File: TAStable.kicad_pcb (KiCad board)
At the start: 2 copper layers, 20 x 16.5 mm, 12 parts, among them J1 Conn_01x06_Pin, U1 74AHCT1G04, U2 CS2300-CP, U3 74LVC1G14

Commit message: schematic
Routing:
- net /21MHz_IN: track 8.04 -> 6.75 mm
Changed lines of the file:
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@@
   (segment (start 128 98.05) (end 128 99.054) (width 0.254) (layer "F.Cu") (net 7))
   (segment (start 132 96.1) (end 132 94.75) (width 0.25) (layer "F.Cu") (net 8))
+  (segment (start 140.24 98.72) (end 140.375 98.72) (width 0.25) (layer "F.Cu") (net 8))
   (segment (start 130.5 93.25) (end 132 94.75) (width 0.254) (layer "F.Cu") (net 8))
-  (segment (start 137.055 97.5) (end 138.275 98.72) (width 0.25) (layer "F.Cu") (net 8))
   (segment (start 132.55 96.65) (end 132 96.1) (width 0.25) (layer "F.Cu") (net 8))
-  (segment (start 138.275 98.72) (end 140.375 98.72) (width 0.25) (layer "F.Cu") (net 8))
+  (segment (start 139.02 97.5) (end 140.24 98.72) (width 0.25) (layer "F.Cu") (net 8))
   (segment (start 128 93.25) (end 130.5 93.25) (width 0.254) (layer "F.Cu") (net 8))
-  (segment (start 135.3 97.5) (end 137.055 97.5) (width 0.25) (layer "F.Cu") (net 8))
   (segment (start 127 94.25) (end 128 93.25) (width 0.254) (layer "F.Cu") (net 8))
   (segment (start 132.55 96.65) (end 134.05 96.65) (width 0.25) (layer "F.Cu") (net 8))
   (segment (start 127 98.05) (end 127 94.25) (width 0.254) (layer "F.Cu") (net 8))
   (segment (start 135.405 97.395) (end 135.3 97.5) (width 0.25) (layer "F.Cu") (net 8))
+  (segment (start 135.3 97.5) (end 139.02 97.5) (width 0.25) (layer "F.Cu") (net 8))
   (segment (start 134.05 96.65) (end 134.795 97.395) (width 0.25) (layer "F.Cu") (net 8))
-  (segment (start 136.4 100.4) (end 136.4 102.6) (width 0.254) (layer "F.Cu") (net 9))
-  (segment (start 138.275 103.8) (end 140.375 103.8) (width 0.25) (layer "F.Cu") (net 9))
-  (segment (start 136.4 102.6) (end 137.6 103.8) (width 0.254) (layer "F.Cu") (net 9))
-  (segment (start 136 100) (end 136.4 100.4) (width 0.254) (layer "F.Cu") (net 9))
-  (segment (start 135.2 100) (end 136 100) (width 0.254) (layer "F.Cu") (net 9))
-  (segment (start 137.6 103.8) (end 138.275 103.8) (width 0.254) (layer "F.Cu") (net 9))
+  (segment (start 140.3 103.8) (end 140.375 103.8) (width 0.25) (layer "F.Cu") (net 9))
+  (segment (start 136.37 100) (end 135.2 100) (width 0.254) (layer "F.Cu") (net 9))
+  (segment (start 136.37 100) (end 136.5 100) (width 0.25) (layer "F.Cu") (net 9))
+  (segment (start 136.5 100) (end 140.3 103.8) (width 0.25) (layer "F.Cu") (net 9))
   (segment (start 131.25 96.5) (end 131.25 95) (width 0.25) (layer "F.Cu") (net 10))
-  (segment (start 136.5 99.5) (end 135.5 98.5) (width 0.25) (layer "F.Cu") (net 10))
-  (segment (start 138.275 101.26) (end 136.515 99.5) (width 0.25) (layer "F.Cu") (net 10))
   (segment (start 133.45 97.5) (end 133.3 97.5) (width 0.25) (layer "F.Cu") (net 10))
+  (segment (start 137.39 98.55) (end 134.35 98.55) (width 0.25) (layer "F.Cu") (net 10))
+  (segment (start 140.375 101.26) (end 140.1 101.26) (width 0.25) (layer "F.Cu") (net 10))
   (segment (start 127.5 94.75) (end 127.5 98.05) (width 0.25) (layer "F.Cu") (net 10))
-  (segment (start 136.515 99.5) (end 136.5 99.5) (width 0.25) (layer "F.Cu") (net 10))
-  (segment (start 133.75 97.5) (end 133.3 97.5) (width 0.25) (layer "F.Cu") (net 10))
+  (segment (start 134.35 98.55) (end 133.3 97.5) (width 0.25) (layer "F.Cu") (net 10))
   (segment (start 130 93.75) (end 128.5 93.75) (width 0.25) (layer "F.Cu") (net 10))
-  (segment (start 138.275 101.26) (end 140.375 101.26) (width 0.25) (layer "F.Cu") (net 10))
   (segment (start 128.5 93.75) (end 127.5 94.75) (width 0.25) (layer "F.Cu") (net 10))
-  (segment (start 134.75 98.5) (end 133.75 97.5) (width 0.25) (layer "F.Cu") (net 10))
-  (segment (start 135.5 98.5) (end 134.75 98.5) (width 0.25) (layer "F.Cu") (net 10))
   (segment (start 133.3 97.5) (end 132.25 97.5) (width 0.25) (layer "F.Cu") (net 10))
   (segment (start 132.25 97.5) (end 131.25 96.5) (width 0.25) (layer "F.Cu") (net 10))
   (segment (start 131.25 95) (end 130 93.75) (width 0.25) (layer "F.Cu") (net 10))
-  (segment (start 135.15 104.8) (end 136.69 106.34) (width 0.254) (layer "F.Cu") (net 11))
-  (segment (start 136.69 106.34) (end 140.375 106.34) (width 0.254) (layer "F.Cu") (net 11))
+  (segment (start 140.1 101.26) (end 137.39 98.55) (width 0.25) (layer "F.Cu") (net 10))
+  (segment (start 135.15 104.8) (end 138.6 104.8) (width 0.254) (layer "F.Cu") (net 11))
+  (segment (start 138.6 104.8) (end 140.14 106.34) (width 0.254) (layer "F.Cu") (net 11))
+  (segment (start 140.14 106.34) (end 140.375 106.34) (width 0.254) (layer "F.Cu") (net 11))
   (zone (net 2) (net_name "GND") (layer "B.Cu") (hatch edge 0.5)
     (connect_pads (clearance 0.5))

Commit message: cleanups
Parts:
- moved C1 0.25 mm to (129.2, 96.0)
- moved C2 0.25 mm to (127.8, 105.5)
- moved C3 0.25 mm to (131.5, 106.0)
- moved C4 0.25 mm to (134.4, 103.1)
- moved C5 0.25 mm to (134.5, 93.2)
- moved R1 0.25 mm to (135.3, 96.9)
- moved R2 0.25 mm to (133.3, 96.9)
- moved R3 0.25 mm to (131.2, 99.5)
- moved U1 0.25 mm to (134.5, 106.0)
- moved U2 0.25 mm to (128.0, 100.5)
- moved U3 0.25 mm to (134.2, 100.2)
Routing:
- net +3.3V: track 61.0 -> 60.2 mm
- added copper zone on F.Cu, net GND

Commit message: code!
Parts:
- added C6: 22uF Tantalum, Capacitor_SMD:C_1206_3216Metric, F.Cu at (125.2, 98.2)
- added C7: 1uF, Capacitor_SMD:C_0603_1608Metric, F.Cu at (129.8, 107.2)
- added C8: 100nF, Capacitor_SMD:C_0603_1608Metric, F.Cu at (121.0, 107.2)
- added J2: ICSP, Connector_PinSocket_2.54mm:PinSocket_1x05_P2.54mm_Vertical, F.Cu at (120.2, 103.2)
- added U4: PIC16LF15313, Package_SO:SOIC-8_3.9x4.9mm_P1.27mm, F.Cu at (125.5, 104.2)
- added U6: AZ1117-3.3, Package_TO_SOT_SMD:SOT-89-3, F.Cu at (125.0, 94.2)
- U1: value 74AHCT1G04 -> 74HCT1G04
- moved C5 2.76 mm to (137.2, 93.5), turned to -90 degrees
- moved U2 2.25 mm to (130.2, 100.5)
- moved C2 2.06 mm to (129.8, 105.0)
- moved C1 2.00 mm to (131.2, 96.0)
- moved C3 2.00 mm to (133.5, 106.0)
- moved C4 2.00 mm to (136.4, 103.1)
- moved R3 2.00 mm to (133.2, 99.5)
- moved U1 2.00 mm to (136.5, 106.0)
- moved U3 2.00 mm to (136.2, 100.2)
- moved R1 1.70 mm to (137.0, 97.0), turned to 90 degrees
- moved R2 1.16 mm to (134.0, 96.0), turned to 90 degrees
- moved J1 0.88 mm to (141.2, 93.7)
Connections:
- C5 pad 1: +3.3V -> +5V
- J1 pad 1: +3.3V -> +5V
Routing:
- net /I2C_SCL: track 20.6 -> 38.9 mm, vias 0 -> 1
- net +5V: track 0.00 -> 13.8 mm
- net /ICSPDAT: track 0.00 -> 11.4 mm, vias 0 -> 1
- net /MCLR: track 0.00 -> 10.3 mm, vias 0 -> 1
- net GND: track 21.8 -> 25.4 mm, vias 5 -> 11
- net /I2C_SDA: track 20.2 -> 23.1 mm
- net Net-(J1-Pin_6): track 5.76 -> 4.25 mm
- net /21MHz_IN: track 6.65 -> 5.33 mm
- net +3.3V: track 60.2 -> 59.3 mm
- net Net-(U2-CLK_IN): track 7.04 -> 6.24 mm
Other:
- board size 20 x 16.5 mm -> 26.8 x 16.5 mm
- board text added: "+"
- board text added: "C"
- board text added: "D"
- board text added: "O"
- board text added: "github/ rasteri/ TAStable"

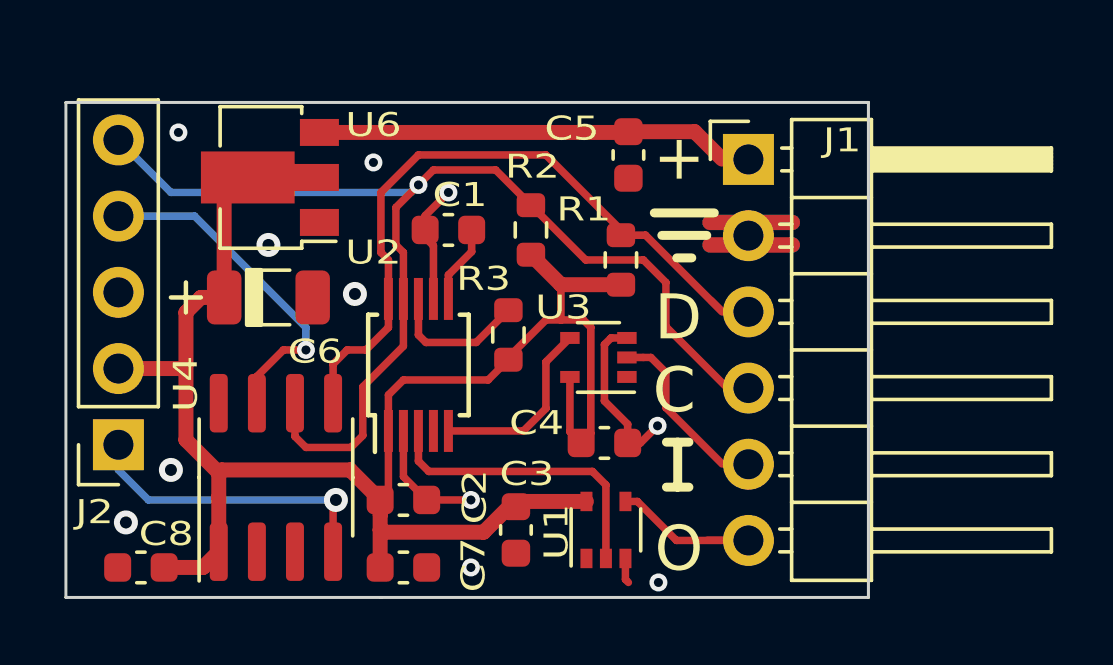
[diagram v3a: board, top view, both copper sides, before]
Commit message: 5v output buffer
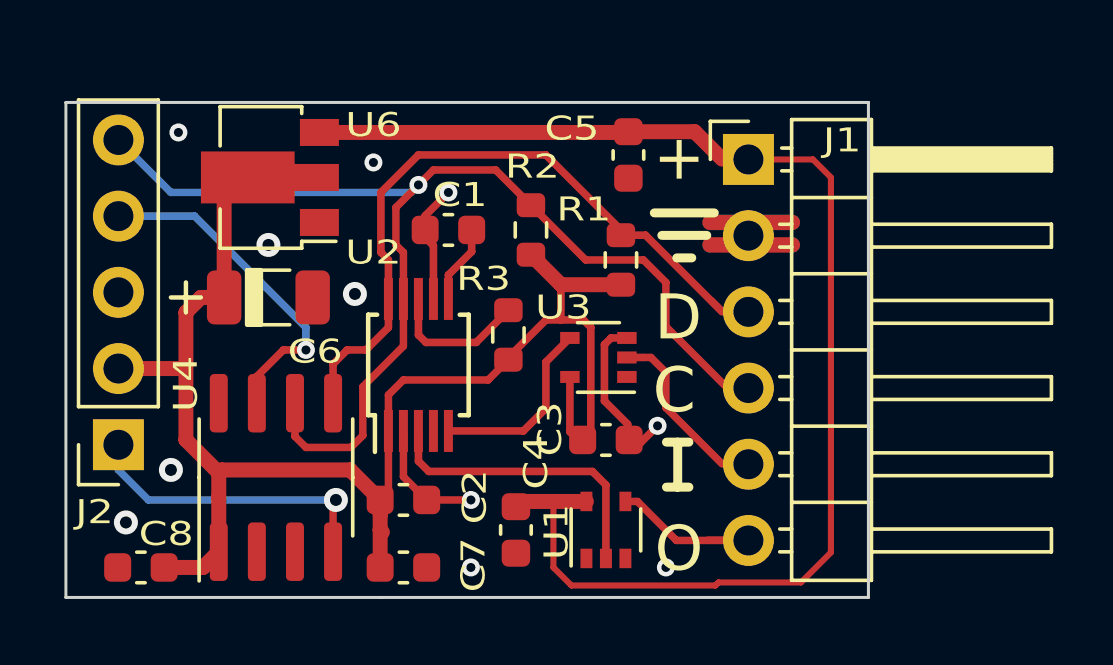
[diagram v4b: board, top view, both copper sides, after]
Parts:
- moved C3 4.24 mm to (136.5, 103.0), turned to 0 degrees
- moved C4 4.14 mm to (133.5, 106.0), turned to -90 degrees
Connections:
- C4 pad 1: +3.3V -> +5V
- J1 pad 3: /I2C_SDA -> /I2C_SCL
- R1 pad 2: /I2C_SDA -> /I2C_SCL
- U1 pad 5: +3.3V -> +5V
- U2 pad 10: /I2C_SDA -> /I2C_SCL
- U4 pad 5: /I2C_SDA -> /I2C_SCL
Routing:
- net +5V: track 13.8 -> 43.9 mm
- net /I2C_SCL: track 38.9 -> 62.0 mm
- net /I2C_SDA: track 23.1 -> 0.00 mm
- net +3.3V: track 59.3 -> 52.1 mm
- net GND: track 25.4 -> 24.6 mm

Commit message: Board pic
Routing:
- net GND: track 24.6 -> 23.4 mm, vias 11 -> 14

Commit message: more pics + cleanups
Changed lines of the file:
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@@
     (property "ki_keywords" "cap capacitor")
     (attr smd)
-    (fp_text reference "C4" (at -2.5 0 90) (layer "F.SilkS")
+    (fp_text reference "C4" (at -2.5 0.25 90) (layer "F.SilkS")
         (effects (font (size 0.8 1) (thickness 0.15)))
     )

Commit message: schematic
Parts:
- J1: value Conn_01x06_Pin -> IN/OUT
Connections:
- net Net-(J1-Pin_6) renamed /24MHz_OUT
- J1 pad 3: /I2C_SCL -> /I2C_SDA
- R1 pad 2: /I2C_SCL -> /I2C_SDA
- U2 pad 10: /I2C_SCL -> /I2C_SDA
- U4 pad 5: /I2C_SCL -> /I2C_SDA
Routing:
- net /I2C_SCL: track 61.8 -> 38.7 mm
- net /I2C_SDA: track 0.00 -> 23.1 mm
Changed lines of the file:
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@@
   (net 8 "/21MHz_IN")
   (net 9 "/I2C_SCL")
-  (net 10 "Net-(J1-Pin_6)")
+  (net 10 "/I2C_SDA")
   (net 11 "unconnected-(U4-RA5-Pad2)")
   (net 12 "unconnected-(U4-RA4-Pad3)")
@@
   (net 14 "/MCLR")
   (net 15 "/ICSPDAT")
+  (net 16 "/24MHz_OUT")
   (footprint "Package_SO:MSOP-10_3x3mm_P0.5mm" (layer "F.Cu")
     (at 130.25 100.5 90)
@@
       (net 9 "/I2C_SCL") (pinfunction "SCL/CCLK") (pintype "input"))
     (pad "10" smd rect (at 2.2 -1 90) (size 1.4 0.3) (layers "F.Cu" "F.Paste" "F.Mask")
-      (net 9 "/I2C_SCL") (pinfunction "SDA/CDIN") (pintype "bidirectional"))
+      (net 10 "/I2C_SDA") (pinfunction "SDA/CDIN") (pintype "bidirectional"))
     (model "${KICAD6_3DMODEL_DIR}/Package_SO.3dshapes/MSOP-10_3x3mm_P0.5mm.wrl"
       (offset (xyz 0 0 0))
@@
         (effects (font (size 0.8 1) (thickness 0.15)))
     )
-    (fp_text value "Conn_01x06_Pin" (at 1.865 16.18) (layer "F.Fab")
+    (fp_text value "IN/OUT" (at 1.865 16.18) (layer "F.Fab")
         (effects (font (size 0.8 1) (thickness 0.15)))
     )
@@
       (net 2 "GND") (pinfunction "Pin_2") (pintype "passive"))
     (pad "3" thru_hole oval (at 0 5.08) (size 1.7 1.7) (drill 1) (layers "*.Cu" "*.Mask")
-      (net 9 "/I2C_SCL") (pinfunction "Pin_3") (pintype "passive"))
+      (net 10 "/I2C_SDA") (pinfunction "Pin_3") (pintype "passive"))
     (pad "4" thru_hole oval (at 0 7.62) (size 1.7 1.7) (drill 1) (layers "*.Cu" "*.Mask")
       (net 9 "/I2C_SCL") (pinfunction "Pin_4") (pintype "passive"))
@@
       (net 8 "/21MHz_IN") (pinfunction "Pin_5") (pintype "passive"))
     (pad "6" thru_hole oval (at 0 12.7) (size 1.7 1.7) (drill 1) (layers "*.Cu" "*.Mask")
-      (net 10 "Net-(J1-Pin_6)") (pinfunction "Pin_6") (pintype "passive"))
+      (net 16 "/24MHz_OUT") (pinfunction "Pin_6") (pintype "passive"))
     (model "${KICAD6_3DMODEL_DIR}/Connector_PinHeader_2.54mm.3dshapes/PinHeader_1x06_P2.54mm_Horizontal.wrl"
       (offset (xyz 0 0 0))
@@
       (net 14 "/MCLR") (pinfunction "RA3") (pintype "input"))
     (pad "5" smd roundrect (at 2.475 1.905 90) (size 1.95 0.6) (layers "F.Cu" "F.Paste" "F.Mask") (roundrect_rratio 0.25)
-      (net 9 "/I2C_SCL") (pinfunction "RA2") (pintype "bidirectional"))
+      (net 10 "/I2C_SDA") (pinfunction "RA2") (pintype "bidirectional"))
     (pad "6" smd roundrect (at 2.475 0.635 90) (size 1.95 0.6) (layers "F.Cu" "F.Paste" "F.Mask") (roundrect_rratio 0.25)
       (net 9 "/I2C_SCL") (pinfunction "RA1") (pintype "bidirectional"))
@@
       (net 1 "+3.3V") (pintype "passive"))
     (pad "2" smd roundrect (at 0.825 0 90) (size 0.8 0.95) (layers "F.Cu" "F.Paste" "F.Mask") (roundrect_rratio 0.25)
-      (net 9 "/I2C_SCL") (pintype "passive"))
+      (net 10 "/I2C_SDA") (pintype "passive"))
     (model "${KICAD6_3DMODEL_DIR}/Resistor_SMD.3dshapes/R_0603_1608Metric.wrl"
       (offset (xyz 0 0 0))
@@
       (net 2 "GND") (pinfunction "GND") (pintype "power_in"))
     (pad "4" smd rect (at 0.95 0.65 90) (size 0.65 0.4) (layers "F.Cu" "F.Paste" "F.Mask")
-      (net 10 "Net-(J1-Pin_6)") (pintype "output"))
+      (net 16 "/24MHz_OUT") (pintype "output"))
     (pad "5" smd rect (at 0.95 -0.65 90) (size 0.65 0.4) (layers "F.Cu" "F.Paste" "F.Mask")
       (net 13 "+5V") (pinfunction "VCC") (pintype "power_in"))
@@
   (segment (start 138 100.25) (end 137.75 100.25) (width 0.25) (layer "F.Cu") (net 8))
   (segment (start 139.5 102.925) (end 139.5 101.75) (width 0.25) (layer "F.Cu") (net 8))
-  (segment (start 140.005 98.35) (end 140.375 98.72) (width 0.25) (layer "F.Cu") (net 9))
   (segment (start 129.75 98.3) (end 129.75 99.875) (width 0.25) (layer "F.Cu") (net 9))
   (segment (start 128 103.25) (end 126.5 103.25) (width 0.25) (layer "F.Cu") (net 9))
   (segment (start 130.25 94.5) (end 129.5 95.25) (width 0.25) (layer "F.Cu") (net 9))
-  (segment (start 130.25 93.5) (end 134.5 93.5) (width 0.254) (layer "F.Cu") (net 9))
   (segment (start 129.5 95.25) (end 129.5 96.5) (width 0.25) (layer "F.Cu") (net 9))
   (segment (start 140.54875 101.27) (end 141.25 101.27) (width 0.25) (layer "F.Cu") (net 9))
-  (segment (start 127.405 100.47) (end 127.875 100) (width 0.254) (layer "F.Cu") (net 9))
   (segment (start 138.5 97.75) (end 138.5 99.22125) (width 0.25) (layer "F.Cu") (net 9))
-  (segment (start 127.405 101.775) (end 127.405 100.47) (width 0.254) (layer "F.Cu") (net 9))
-  (segment (start 129 96.75) (end 129 94.75) (width 0.254) (layer "F.Cu") (net 9))
-  (segment (start 127.875 100) (end 128.5 100) (width 0.254) (layer "F.Cu") (net 9))
   (segment (start 126.135 102.885) (end 126.135 101.775) (width 0.25) (layer "F.Cu") (net 9))
   (segment (start 137.75 97) (end 138.5 97.75) (width 0.25) (layer "F.Cu") (net 9))
@@
   (segment (start 138.5 99.22125) (end 140.54875 101.27) (width 0.25) (layer "F.Cu") (net 9))
   (segment (start 129.5 96.5) (end 129.75 96.75) (width 0.25) (layer "F.Cu") (net 9))
-  (segment (start 129.25 97) (end 129 96.75) (width 0.254) (layer "F.Cu") (net 9))
-  (segment (start 129 94.75) (end 130.25 93.5) (width 0.254) (layer "F.Cu") (net 9))
-  (segment (start 129.25 99.25) (end 129.25 97) (width 0.254) (layer "F.Cu") (net 9))
   (segment (start 126.5 103.25) (end 126.135 102.885) (width 0.25) (layer "F.Cu") (net 9))
   (segment (start 129.75 99.875) (end 128.396838 101.228162) (width 0.25) (layer "F.Cu") (net 9))
-  (segment (start 134.5 93.5) (end 137.25 96.25) (width 0.254) (layer "F.Cu") (net 9))
-  (segment (start 140.375 98.73) (end 137.82 96.175) (width 0.254) (layer "F.Cu") (net 9))
-  (segment (start 137.82 96.175) (end 137 96.175) (width 0.254) (layer "F.Cu") (net 9))
   (segment (start 129.75 96.75) (end 129.75 98.3) (width 0.25) (layer "F.Cu") (net 9))
   (segment (start 130.75 94) (end 132.825 94) (width 0.25) (layer "F.Cu") (net 9))
-  (segment (start 128.5 100) (end 129.25 99.25) (width 0.254) (layer "F.Cu") (net 9))
   (via (at 130.25 94.5) (size 0.6) (drill 0.3) (layers "F.Cu" "B.Cu") (net 9))
   (segment (start 130.25 94.5) (end 128 94.5) (width 0.25) (layer "B.Cu") (net 9))
@@
   (segment (start 121.25 93) (end 120.25 93) (width 0.25) (layer "B.Cu") (net 9))
   (segment (start 128 94.5) (end 127.25 93.75) (width 0.25) (layer "B.Cu") (net 9))
-  (segment (start 141.25 106.35) (end 141.24 106.34) (width 0.254) (layer "F.Cu") (net 10))
-  (segment (start 137.15 105.05) (end 138.3 105.05) (width 0.25) (layer "F.Cu") (net 10))
-  (segment (start 138.3 105.05) (end 139.6 106.35) (width 0.25) (layer "F.Cu") (net 10))
-  (segment (start 139.6 106.35) (end 140.375 106.35) (width 0.25) (layer "F.Cu") (net 10))
+  (segment (start 140.005 98.35) (end 140.375 98.72) (width 0.25) (layer "F.Cu") (net 10))
+  (segment (start 130.25 93.5) (end 134.5 93.5) (width 0.254) (layer "F.Cu") (net 10))
+  (segment (start 127.405 100.47) (end 127.875 100) (width 0.254) (layer "F.Cu") (net 10))
+  (segment (start 127.405 101.775) (end 127.405 100.47) (width 0.254) (layer "F.Cu") (net 10))
+  (segment (start 129 96.75) (end 129 94.75) (width 0.254) (layer "F.Cu") (net 10))
+  (segment (start 127.875 100) (end 128.5 100) (width 0.254) (layer "F.Cu") (net 10))
+  (segment (start 129.25 97) (end 129 96.75) (width 0.254) (layer "F.Cu") (net 10))
+  (segment (start 129 94.75) (end 130.25 93.5) (width 0.254) (layer "F.Cu") (net 10))
+  (segment (start 129.25 99.25) (end 129.25 97) (width 0.254) (layer "F.Cu") (net 10))
+  (segment (start 134.5 93.5) (end 137.25 96.25) (width 0.254) (layer "F.Cu") (net 10))
+  (segment (start 140.375 98.73) (end 137.82 96.175) (width 0.254) (layer "F.Cu") (net 10))
+  (segment (start 137.82 96.175) (end 137 96.175) (width 0.254) (layer "F.Cu") (net 10))
+  (segment (start 128.5 100) (end 129.25 99.25) (width 0.254) (layer "F.Cu") (net 10))
   (segment (start 137.225 92.75) (end 126.95 92.75) (width 0.5) (layer "F.Cu") (net 13))
   (segment (start 139.46 92.725) (end 140.375 93.64) (width 0.5) (layer "F.Cu") (net 13))
@@
   (segment (start 125.25 96) (end 120.71 96) (width 0.254) (layer "B.Cu") (net 15))
   (segment (start 120.71 96) (end 120.25 95.54) (width 0.254) (layer "B.Cu") (net 15))
+  (segment (start 141.25 106.35) (end 141.24 106.34) (width 0.254) (layer "F.Cu") (net 16))
+  (segment (start 137.15 105.05) (end 138.3 105.05) (width 0.25) (layer "F.Cu") (net 16))
+  (segment (start 138.3 105.05) (end 139.6 106.35) (width 0.25) (layer "F.Cu") (net 16))
+  (segment (start 139.6 106.35) (end 140.375 106.35) (width 0.25) (layer "F.Cu") (net 16))
   (zone (net 2) (net_name "GND") (layers "F&B.Cu") (hatch edge 0.5)
     (connect_pads (clearance 0.5))
